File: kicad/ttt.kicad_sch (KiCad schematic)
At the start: 33 parts, among them SW1 SW_Push, SW10 SW_Slide_DPDT, SW2 SW_Push, SW3 SW_Push, SW4 SW_Push, SW5 SW_Push, SW6 SW_Push, SW7 SW_Push, SW8 SW_Push, SW9 SW_Push

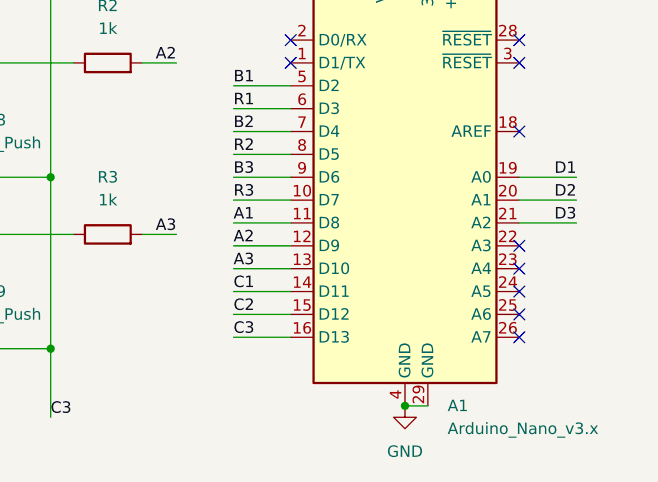
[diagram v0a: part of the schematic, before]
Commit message: Update configuration and build scripts for AVR target; modify KiCad schematic and main.rs button configuration
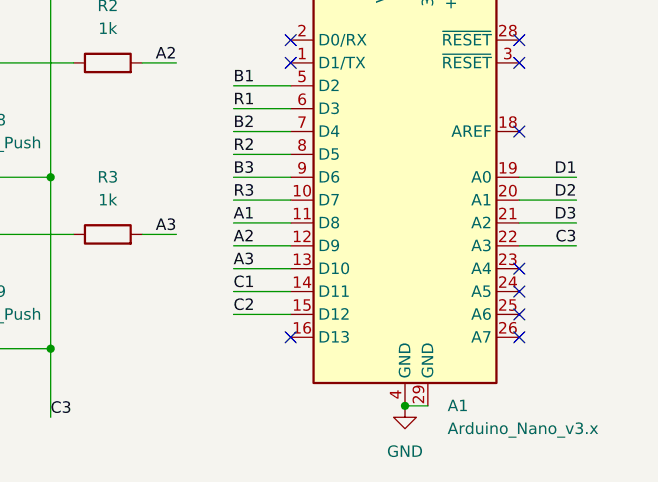
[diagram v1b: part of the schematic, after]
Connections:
- net C3: now also A1.22 (A3); no longer A1.16 (D13)
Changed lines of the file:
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@@
-	)
-	(no_connect
-		(at 212.09 102.87)
 	)
 	(no_connect
@@
 		(at 212.09 80.01)
 	)
+	(no_connect
+		(at 186.69 113.03)
+	)
 	(wire
 		(pts
@@
 	(wire
 		(pts
-			(xy 180.34 113.03) (xy 186.69 113.03)
+			(xy 218.44 102.87) (xy 212.09 102.87)
 		)
 		(stroke
@@
 	)
 	(label "C3"
-		(at 180.34 113.03 0)
+		(at 218.44 102.87 180)
 		(fields_autoplaced yes)
 		(effects
@@
 				(size 1.27 1.27)
 			)
-			(justify left bottom)
-		)
-	)
+			(justify right bottom)
+		)
+	)
